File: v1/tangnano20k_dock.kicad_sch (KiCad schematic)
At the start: 54 parts, among them J1 Mini-DIN-6, J2 Conn_01x02, J3 DB15_Female_HighDensity_Mount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, J4 DB9_Male, J5 Conn_02x10_Odd_Even, J6 Conn_02x10_Odd_Even, J7 RCA, J8 FCR684205T, J9 AudioJack3, U1 TXS0104E, U2 TangNano20K, U3 CS4354

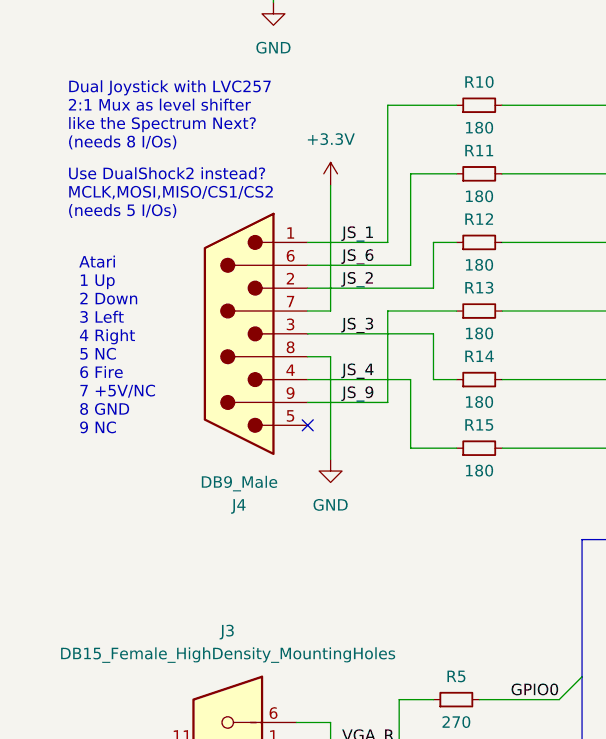
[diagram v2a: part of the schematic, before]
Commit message: Corrected Joystick footprint
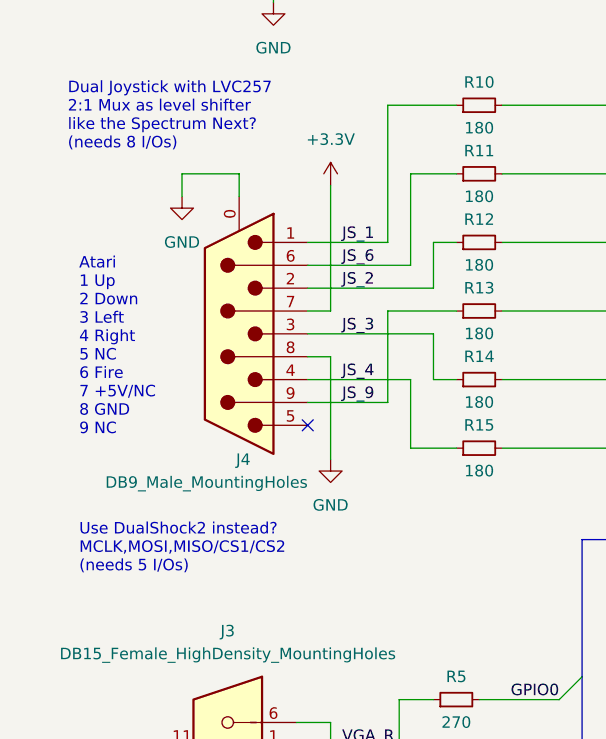
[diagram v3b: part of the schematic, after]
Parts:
- removed J4: DB9_Male, Connector_Dsub:DSUB-9_Male_Horizontal_P2.77x2.54mm_EdgePinOffset9.40mm, symbol Connector:DB9_Male
- added J4: DB9_Male_MountingHoles, Connector_Dsub:DSUB-9_Male_Horizontal_P2.77x2.84mm_EdgePinOffset7.70mm_Housed_MountingHolesOffset9.12mm, symbol Connector:DB9_Male_MountingHoles
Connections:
- net +3.3V: now also J4.7
- net GND: now also J4.0 (PAD), J4.8
- net JS_1: now also J4.1
- net JS_2: now also J4.2
- net JS_3: now also J4.3
- net JS_4: now also J4.4
- net JS_6: now also J4.6
- net JS_9: now also J4.9
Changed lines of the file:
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@@
   (junction (at 222.25 73.66) (diameter 0) (color 0 0 0 0)
   )
-  (junction (at 44.45 179.07) (diameter 0) (color 0 0 0 0)
-  )
   (junction (at 265.43 87.63) (diameter 0) (color 0 0 0 0)
   )
@@
   (junction (at 44.45 173.99) (diameter 0) (color 0 0 0 0)
   )
+  (junction (at 44.45 179.07) (diameter 0) (color 0 0 0 0)
+  )
   (junction (at 44.45 158.75) (diameter 0) (color 0 0 0 0)
   )
@@
     (stroke (width 0) (type default) (color 0 0 0 0))
   )
+  (wire (pts (xy 27.94 92.71) (xy 34.29 92.71))
+    (stroke (width 0) (type default) (color 0 0 0 0))
+  )
   (wire (pts (xy 195.58 129.54) (xy 180.34 129.54))
     (stroke (width 0) (type default) (color 0 0 0 0))
@@
     (stroke (width 0) (type default) (color 0 0 0 0))
   )
-  (wire (pts (xy 33.02 184.15) (xy 40.64 184.15))
-    (stroke (width 0) (type default) (color 0 0 0 0))
-  )
   (wire (pts (xy 63.5 100.33) (xy 83.82 100.33))
     (stroke (width 0) (type default) (color 0 0 0 0))
@@
     (stroke (width 0) (type default) (color 0 0 0 0))
   )
+  (wire (pts (xy 34.29 92.71) (xy 34.29 95.25))
+    (stroke (width 0) (type default) (color 0 0 0 0))
+  )
   (wire (pts (xy 44.45 173.99) (xy 44.45 176.53))
     (stroke (width 0) (type default) (color 0 0 0 0))
@@
     (stroke (width 0) (type default) (color 0 0 0 0))
   )
+  (wire (pts (xy 33.02 184.15) (xy 40.64 184.15))
+    (stroke (width 0) (type default) (color 0 0 0 0))
+  )
   (wire (pts (xy 240.03 21.59) (xy 240.03 20.32))
     (stroke (width 0) (type default) (color 0 0 0 0))
@@
     (stroke (width 0) (type default) (color 0 0 0 0))
   )
+  (wire (pts (xy 44.45 179.07) (xy 44.45 181.61))
+    (stroke (width 0) (type default) (color 0 0 0 0))
+  )
   (wire (pts (xy 203.2 151.13) (xy 208.28 151.13))
     (stroke (width 0) (type default) (color 0 0 0 0))
@@
     (stroke (width 0) (type default) (color 0 0 0 0))
   )
+  (wire (pts (xy 40.64 179.07) (xy 44.45 179.07))
+    (stroke (width 0) (type default) (color 0 0 0 0))
+  )
   (wire (pts (xy 203.2 104.14) (xy 212.09 104.14))
     (stroke (width 0) (type default) (color 0 0 0 0))
@@
     (stroke (width 0) (type default) (color 0 0 0 0))
   )
+  (wire (pts (xy 27.94 95.25) (xy 27.94 92.71))
+    (stroke (width 0) (type default) (color 0 0 0 0))
+  )
   (bus (pts (xy 127 153.67) (xy 127 167.64))
     (stroke (width 0) (type default) (color 0 0 0 0))
@@
     (stroke (width 0) (type default) (color 0 0 0 0))
   )
-  (wire (pts (xy 44.45 179.07) (xy 44.45 181.61))
+  (wire (pts (xy 44.45 176.53) (xy 44.45 179.07))
     (stroke (width 0) (type default) (color 0 0 0 0))
   )
@@
     (stroke (width 0) (type default) (color 0 0 0 0))
   )
-  (wire (pts (xy 44.45 176.53) (xy 44.45 179.07))
-    (stroke (width 0) (type default) (color 0 0 0 0))
-  )
   (wire (pts (xy 119.38 68.58) (xy 142.24 68.58))
     (stroke (width 0) (type default) (color 0 0 0 0))
@@
     (stroke (width 0) (type default) (color 0 0 0 0))
   )
-  (wire (pts (xy 40.64 179.07) (xy 44.45 179.07))
+  (wire (pts (xy 40.64 184.15) (xy 40.64 179.07))
     (stroke (width 0) (type default) (color 0 0 0 0))
   )
@@
     (stroke (width 0) (type default) (color 0 0 0 0))
   )
-  (wire (pts (xy 40.64 184.15) (xy 40.64 179.07))
-    (stroke (width 0) (type default) (color 0 0 0 0))
-  )
   (bus (pts (xy 127 91.44) (xy 127 96.52))
     (stroke (width 0) (type default) (color 0 0 0 0))
@@
   )
   (text "Use DualShock2 instead?\nMCLK,MOSI,MISO/CS1/CS2\n(needs 5 I/Os)"
-    (at 15.24 97.79 0)
+    (at 16.51 137.16 0)
     (effects (font (size 1.27 1.27)) (justify left bottom))
   )
@@
     (pin "2")
   )
+  (symbol (lib_id "power:GND") (at 27.94 95.25 0) (unit 1)
+    (in_bom yes) (on_board yes) (fields_autoplaced)
+    (property "Reference" "#PWR?" (id 0) (at 27.94 101.6 0)
+      (effects (font (size 1.27 1.27)) hide)
+    )
+    (property "Value" "GND" (id 1) (at 27.94 100.33 0))
+    (property "Footprint" "" (id 2) (at 27.94 95.25 0)
+      (effects (font (size 1.27 1.27)) hide)
+    )
+    (property "Datasheet" "" (id 3) (at 27.94 95.25 0)
+      (effects (font (size 1.27 1.27)) hide)
+    )
+    (pin "1")
+  )
   (symbol (lib_id "Connector:AudioJack3") (at 278.13 109.22 180) (unit 1)
     (in_bom yes) (on_board yes)
@@
     (pin "1")
   )
+  (symbol (lib_id "Connector:DB9_Male_MountingHoles") (at 34.29 110.49 180) (unit 1)
+    (in_bom yes) (on_board yes)
+    (property "Reference" "J4" (id 0) (at 35.56 124.46 0)
+      (effects (font (size 1.27 1.27)) (justify left))
+    )
+    (property "Value" "DB9_Male_MountingHoles" (id 1) (at 41.91 127 0)
+      (effects (font (size 1.27 1.27)) (justify left))
+    )
+    (property "Footprint" "Connector_Dsub:DSUB-9_Male_Horizontal_P2.77x2.84mm_EdgePinOffset7.70mm_Housed_MountingHolesOffset9.12mm" (id 2) (at 34.29 110.49 0)
+      (effects (font (size 1.27 1.27)) hide)
+    )
+    (property "Datasheet" " ~" (id 3) (at 34.29 110.49 0)
+      (effects (font (size 1.27 1.27)) hide)
+    )
+    (pin "0")
+    (pin "1")
+    (pin "2")
+    (pin "3")
+    (pin "4")
+    (pin "5")
+    (pin "6")
+    (pin "7")
+    (pin "8")
+    (pin "9")
+  )
   (symbol (lib_id "Device:R_Small") (at 60.96 100.33 90) (unit 1)
     (in_bom yes) (on_board yes)
@@
     (pin "9")
   )
-  (symbol (lib_id "Connector:DB9_Male") (at 34.29 110.49 180) (unit 1)
-    (in_bom yes) (on_board yes) (fields_autoplaced)
-    (property "Reference" "J4" (id 0) (at 34.29 129.54 0))
-    (property "Value" "DB9_Male" (id 1) (at 34.29 127 0))
-    (property "Footprint" "Connector_Dsub:DSUB-9_Male_Horizontal_P2.77x2.54mm_EdgePinOffset9.40mm" (id 2) (at 34.29 110.49 0)
-      (effects (font (size 1.27 1.27)) hide)
-    )
-    (property "Datasheet" " ~" (id 3) (at 34.29 110.49 0)
-      (effects (font (size 1.27 1.27)) hide)
-    )
-    (pin "1")
-    (pin "2")
-    (pin "3")
-    (pin "4")
-    (pin "5")
-    (pin "6")
-    (pin "7")
-    (pin "8")
-    (pin "9")
-  )
   (symbol (lib_id "power:GND") (at 33.02 30.48 0) (mirror x) (unit 1)
     (in_bom yes) (on_board yes) (fields_autoplaced)
@@
       (reference "#PWR0106") (unit 1) (value "GND") (footprint "")
     )
+    (path "/483f4ea5-aee5-4e65-a228-919e59862dcf"
+      (reference "#PWR?") (unit 1) (value "GND") (footprint "")
+    )
     (path "/1fd682e2-38d3-4e6f-9b3a-e87d3b2b467c"
       (reference "C1") (unit 1) (value "100n") (footprint "Capacitor_THT:C_Disc_D4.3mm_W1.9mm_P5.00mm")
@@
       (reference "J3") (unit 1) (value "DB15_Female_HighDensity_MountingHoles") (footprint "TangNano20k:DSUB-15-HD_Female_Horizontal_P2.29x1.98mm_EdgePinOffset8.35mm_Housed_MountingHolesOffset10.89mm")
     )
-    (path "/8d13ec8a-0e85-4cb6-815a-22cecb20a93c"
-      (reference "J4") (unit 1) (value "DB9_Male") (footprint "Connector_Dsub:DSUB-9_Male_Horizontal_P2.77x2.54mm_EdgePinOffset9.40mm")
+    (path "/526e9db4-aaf4-4ef6-8bd7-e9a9c144c3d3"
+      (reference "J4") (unit 1) (value "DB9_Male_MountingHoles") (footprint "Connector_Dsub:DSUB-9_Male_Horizontal_P2.77x2.84mm_EdgePinOffset7.70mm_Housed_MountingHolesOffset9.12mm")
     )
     (path "/8bafd92d-67dd-465f-87bc-94be9b0bc7f0"

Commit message: Minor changes
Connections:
- net GPIO3: now also R9.2; no longer R8.2
- net GPIO4: now also R8.2; no longer R9.2
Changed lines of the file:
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@@
     (effects (font (size 1.27 1.27)) (justify right bottom))
   )
-  (label "GPIO3" (at 69.85 181.61 180)
+  (label "GPIO4" (at 69.85 181.61 180)
     (effects (font (size 1.27 1.27)) (justify right bottom))
   )
@@
     (effects (font (size 1.27 1.27)) (justify right bottom))
   )
-  (label "GPIO4" (at 69.85 191.77 180)
+  (label "GPIO3" (at 69.85 191.77 180)
     (effects (font (size 1.27 1.27)) (justify right bottom))
   )
@@
   (symbol (lib_id "power:GND") (at 27.94 95.25 0) (unit 1)
     (in_bom yes) (on_board yes) (fields_autoplaced)
-    (property "Reference" "#PWR?" (id 0) (at 27.94 101.6 0)
+    (property "Reference" "#PWR0107" (id 0) (at 27.94 101.6 0)
       (effects (font (size 1.27 1.27)) hide)
     )
@@
     )
     (path "/483f4ea5-aee5-4e65-a228-919e59862dcf"
-      (reference "#PWR?") (unit 1) (value "GND") (footprint "")
+      (reference "#PWR0107") (unit 1) (value "GND") (footprint "")
     )
     (path "/1fd682e2-38d3-4e6f-9b3a-e87d3b2b467c"
